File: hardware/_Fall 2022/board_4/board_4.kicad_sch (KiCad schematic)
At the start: 9 parts, among them J1 Conn_01x04, J2 Conn_01x04, J3 Conn_01x04, U1 Teensy4.1

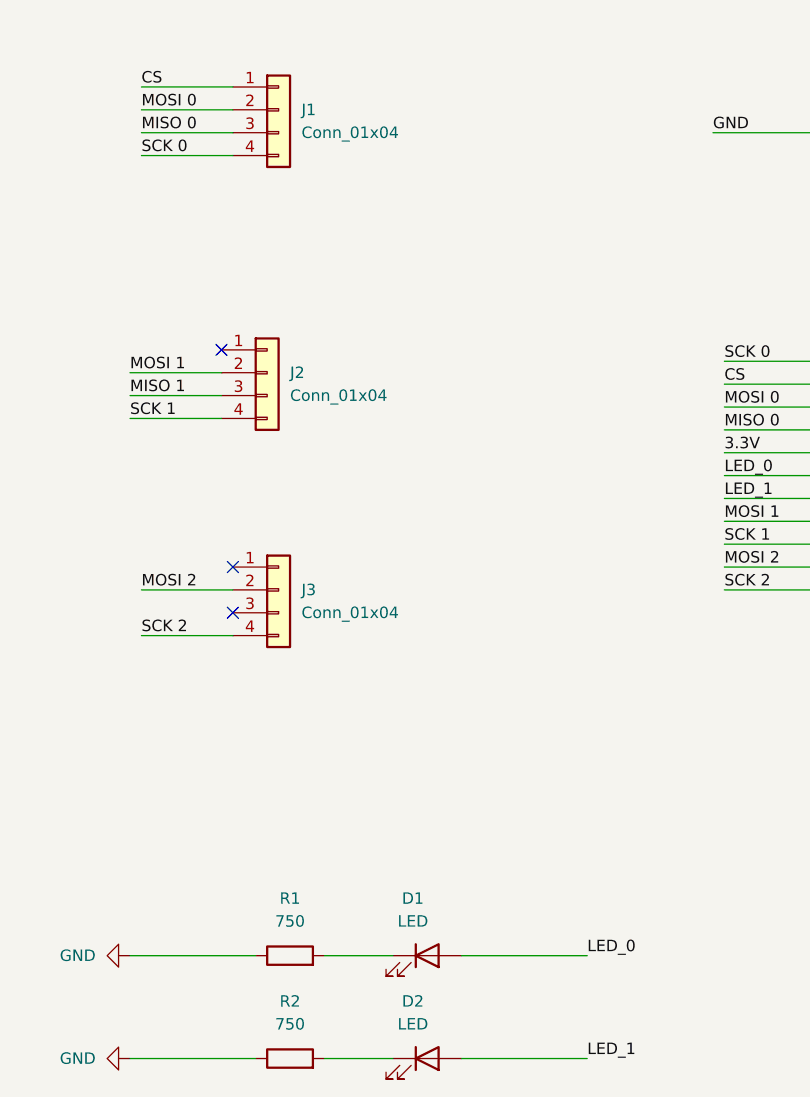
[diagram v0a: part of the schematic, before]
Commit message: Update schematics for both Teensy board schematics
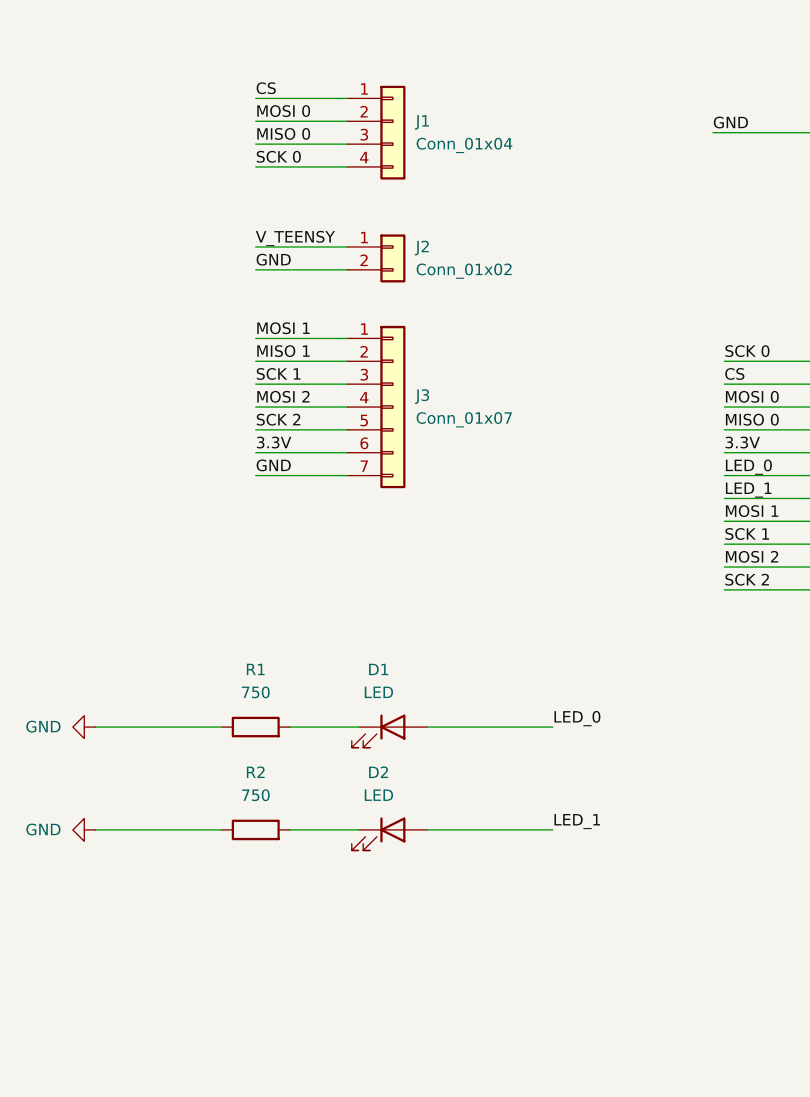
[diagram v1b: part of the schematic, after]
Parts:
- removed J2, J3: Conn_01x04, symbol Connector_Generic:Conn_01x04
- added J2: Conn_01x02, symbol Connector_Generic:Conn_01x02
- added J3: Conn_01x07, symbol Connector_Generic:Conn_01x07
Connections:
- net 3.3V: now also J3.6 (Pin_6)
- net GND: now also J2.2 (Pin_2), J3.7 (Pin_7)
- net MISO 1: now also J3.2 (Pin_2)
- net MOSI 1: now also J3.1 (Pin_1)
- net MOSI 2: now also J3.4 (Pin_4)
- net SCK 1: now also J3.3 (Pin_3)
- net SCK 2: now also J3.5 (Pin_5)
- net V_TEENSY: now also J2.1 (Pin_1)
- no-connect marks 56 -> 53
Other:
- moved on the sheet: D1, D2, J1, R1, R2

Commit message: Add more LED
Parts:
- added D?: LED, symbol Device:LED
- added R?: 750, symbol Device:R
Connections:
- net GND: now also R?.1
- net LED_2: now reaches U1.10 (8_TX2_IN1)
- net LED_2: now also D?.2 (A)
- new net: D?.1 (K), R?.2
- no-connect marks 53 -> 52
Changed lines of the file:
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@@
   (no_connect (at 231.14 46.99))
   (no_connect (at 231.14 64.77))
-  (no_connect (at 175.26 62.23))
   (no_connect (at 231.14 35.56))
   (no_connect (at 231.14 85.09))
@@
     (stroke (width 0) (type default) (color 0 0 0 0))
   )
+  (wire (pts (xy 162.56 62.23) (xy 175.26 62.23))
+    (stroke (width 0) (type default) (color 0 0 0 0))
+  )
   (wire (pts (xy 162.56 80.01) (xy 175.26 80.01))
     (stroke (width 0) (type default) (color 0 0 0 0))
@@
     (stroke (width 0) (type default) (color 0 0 0 0))
   )
+  (wire (pts (xy 92.71 128.27) (xy 106.68 128.27))
+    (stroke (width 0) (type default) (color 0 0 0 0))
+  )
   (wire (pts (xy 110.49 38.1) (xy 120.65 38.1))
     (stroke (width 0) (type default) (color 0 0 0 0))
@@
     (stroke (width 0) (type default) (color 0 0 0 0))
   )
+  (wire (pts (xy 114.3 128.27) (xy 121.92 128.27))
+    (stroke (width 0) (type default) (color 0 0 0 0))
+  )
   (wire (pts (xy 92.71 105.41) (xy 106.68 105.41))
     (stroke (width 0) (type default) (color 0 0 0 0))
@@
     (stroke (width 0) (type default) (color 0 0 0 0))
   )
+  (wire (pts (xy 129.54 128.27) (xy 143.51 128.27))
+    (stroke (width 0) (type default) (color 0 0 0 0))
+  )
   (wire (pts (xy 162.56 64.77) (xy 175.26 64.77))
     (stroke (width 0) (type default) (color 0 0 0 0))
@@
     (effects (font (size 1.27 1.27)) (justify left bottom))
   )
+  (label "LED_2" (at 162.56 62.23 0)
+    (effects (font (size 1.27 1.27)) (justify left bottom))
+  )
   (label "LED_0" (at 143.51 105.41 0)
     (effects (font (size 1.27 1.27)) (justify left bottom))
@@
     (effects (font (size 1.27 1.27)) (justify left bottom))
   )
+  (label "LED_2" (at 143.51 128.27 0)
+    (effects (font (size 1.27 1.27)) (justify left bottom))
+  )
   (label "3.3V" (at 110.49 74.93 0)
     (effects (font (size 1.27 1.27)) (justify left bottom))
@@
   (label "SCK 0" (at 110.49 43.18 0)
     (effects (font (size 1.27 1.27)) (justify left bottom))
+  )
+  (symbol (lib_id "Device:R") (at 110.49 128.27 90) (unit 1)
+    (in_bom yes) (on_board yes) (fields_autoplaced)
+    (property "Reference" "R?" (id 0) (at 110.49 121.92 90))
+    (property "Value" "750" (id 1) (at 110.49 124.46 90))
+    (property "Footprint" "" (id 2) (at 110.49 130.048 90)
+      (effects (font (size 1.27 1.27)) hide)
+    )
+    (property "Datasheet" "~" (id 3) (at 110.49 128.27 0)
+      (effects (font (size 1.27 1.27)) hide)
+    )
+    (pin "1")
+    (pin "2")
   )
   (symbol (lib_id "power:GND") (at 92.71 116.84 270) (unit 1)
@@
     )
     (pin "1")
+  )
+  (symbol (lib_id "Device:LED") (at 125.73 128.27 0) (unit 1)
+    (in_bom yes) (on_board yes) (fields_autoplaced)
+    (property "Reference" "D?" (id 0) (at 124.1425 121.92 0))
+    (property "Value" "LED" (id 1) (at 124.1425 124.46 0))
+    (property "Footprint" "" (id 2) (at 125.73 128.27 0)
+      (effects (font (size 1.27 1.27)) hide)
+    )
+    (property "Datasheet" "~" (id 3) (at 125.73 128.27 0)
+      (effects (font (size 1.27 1.27)) hide)
+    )
+    (pin "1")
+    (pin "2")
   )
   (symbol (lib_id "Device:C") (at 264.16 46.99 0) (unit 1)
@@
     (pin "1")
     (pin "2")
+  )
+  (symbol (lib_id "power:GND") (at 92.71 128.27 270) (unit 1)
+    (in_bom yes) (on_board yes) (fields_autoplaced)
+    (property "Reference" "#PWR?" (id 0) (at 86.36 128.27 0)
+      (effects (font (size 1.27 1.27)) hide)
+    )
+    (property "Value" "GND" (id 1) (at 88.9 128.2699 90)
+      (effects (font (size 1.27 1.27)) (justify right))
+    )
+    (property "Footprint" "" (id 2) (at 92.71 128.27 0)
+      (effects (font (size 1.27 1.27)) hide)
+    )
+    (property "Datasheet" "" (id 3) (at 92.71 128.27 0)
+      (effects (font (size 1.27 1.27)) hide)
+    )
+    (pin "1")
   )
   (symbol (lib_id "Teensy:Teensy4.1") (at 203.2 93.98 0) (unit 1)
@@
       (reference "#PWR03") (unit 1) (value "GND") (footprint "")
     )
+    (path "/b12cba0b-0cbd-46bf-980a-723c0f1e7487"
+      (reference "#PWR?") (unit 1) (value "GND") (footprint "")
+    )
     (path "/82e280a4-56a4-4b9c-912d-48b78e5c2f29"
       (reference "C1") (unit 1) (value "0.1uF") (footprint "")
@@
       (reference "D2") (unit 1) (value "LED") (footprint "")
     )
+    (path "/7c62d015-5e28-4052-8778-1850be8e0d5d"
+      (reference "D?") (unit 1) (value "LED") (footprint "")
+    )
     (path "/f852b861-1da2-4c35-8389-6db74b76175d"
       (reference "J1") (unit 1) (value "Conn_01x04") (footprint "")
@@
       (reference "R2") (unit 1) (value "750") (footprint "")
     )
+    (path "/1888f0b4-2d0a-4b9c-a693-44e35b7d42e8"
+      (reference "R?") (unit 1) (value "750") (footprint "")
+    )
     (path "/b2758a0a-4bfb-4a9e-9bf3-46b060736299"

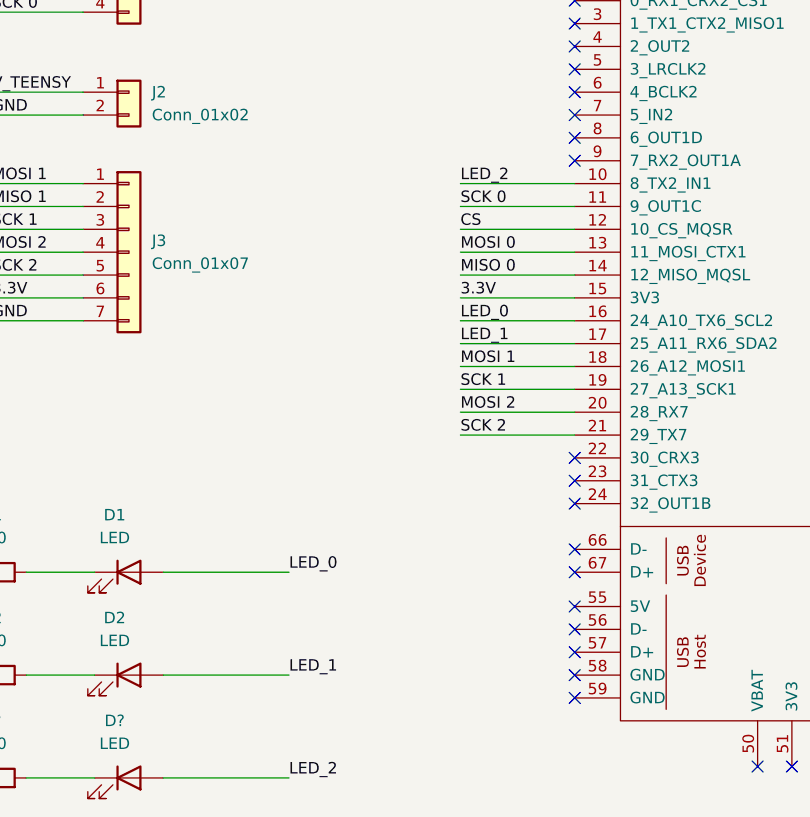
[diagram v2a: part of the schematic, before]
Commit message: Change minor labeling error in teensy boards kicad
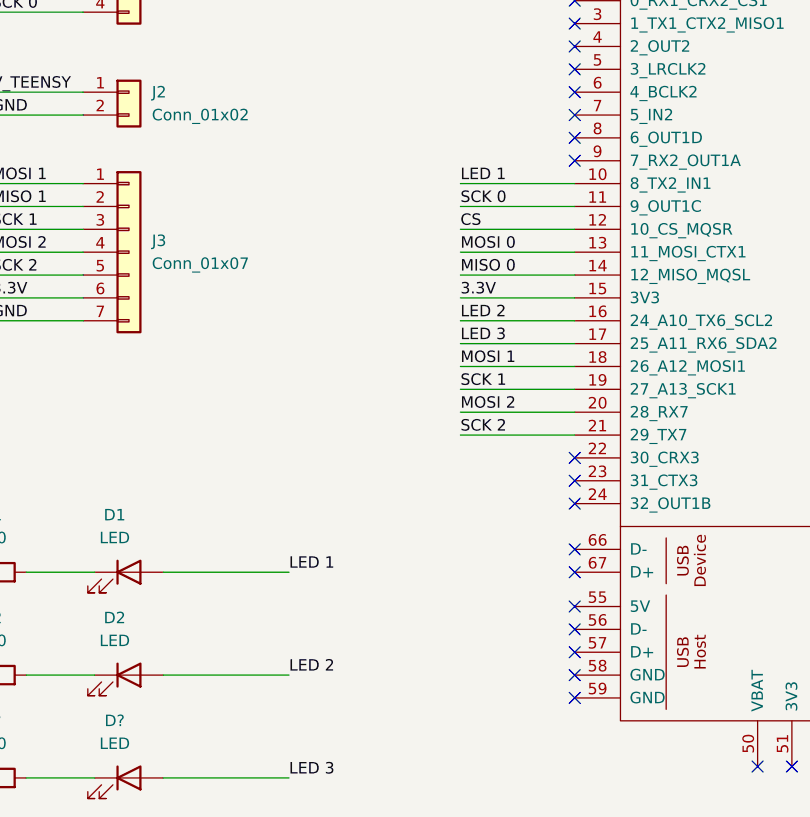
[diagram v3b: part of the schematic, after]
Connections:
- net LED_0 renamed LED 1
- net LED 1: now also U1.10 (8_TX2_IN1); no longer U1.16 (24_A10_TX6_SCL2)
- net LED_1 renamed LED 2
- net LED 2: now also U1.16 (24_A10_TX6_SCL2); no longer U1.17 (25_A11_RX6_SDA2)
- net LED_2 renamed LED 3
- net LED 3: now also U1.17 (25_A11_RX6_SDA2); no longer U1.10 (8_TX2_IN1)
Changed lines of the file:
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@@
     (effects (font (size 1.27 1.27)) (justify left bottom))
   )
-  (label "LED_2" (at 162.56 62.23 0)
+  (label "LED 1" (at 162.56 62.23 0)
     (effects (font (size 1.27 1.27)) (justify left bottom))
   )
-  (label "LED_0" (at 143.51 105.41 0)
+  (label "LED 1" (at 143.51 105.41 0)
     (effects (font (size 1.27 1.27)) (justify left bottom))
   )
@@
     (effects (font (size 1.27 1.27)) (justify left bottom))
   )
-  (label "LED_2" (at 143.51 128.27 0)
+  (label "LED 3" (at 143.51 128.27 0)
     (effects (font (size 1.27 1.27)) (justify left bottom))
   )
@@
     (effects (font (size 1.27 1.27)) (justify left bottom))
   )
-  (label "LED_1" (at 162.56 80.01 0)
+  (label "LED 3" (at 162.56 80.01 0)
     (effects (font (size 1.27 1.27)) (justify left bottom))
   )
@@
     (effects (font (size 1.27 1.27)) (justify left bottom))
   )
-  (label "LED_0" (at 162.56 77.47 0)
+  (label "LED 2" (at 162.56 77.47 0)
     (effects (font (size 1.27 1.27)) (justify left bottom))
   )
@@
     (effects (font (size 1.27 1.27)) (justify left bottom))
   )
-  (label "LED_1" (at 143.51 116.84 0)
+  (label "LED 2" (at 143.51 116.84 0)
     (effects (font (size 1.27 1.27)) (justify left bottom))
   )
